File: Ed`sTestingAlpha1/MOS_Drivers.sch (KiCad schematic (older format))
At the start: 6 parts

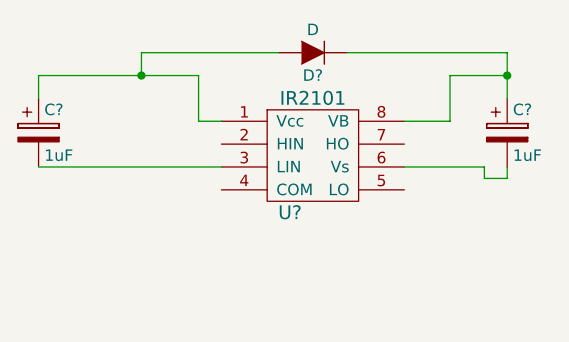
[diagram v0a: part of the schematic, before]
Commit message: Small mods on schematic -- added some pins
Added some docs
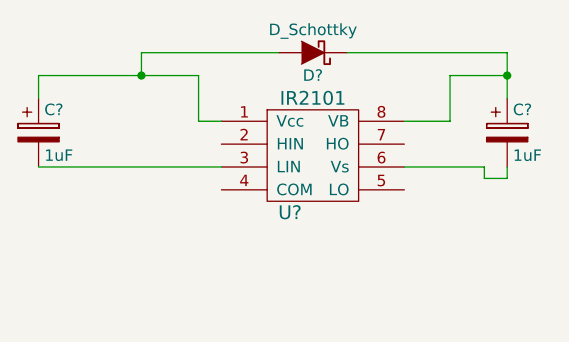
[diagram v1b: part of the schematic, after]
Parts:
- removed D?: D, symbol D
- added D?: D_Schottky, symbol D_Schottky
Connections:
- net at C?.1, U?.1 (Vcc): now also D?.2 (A)
- net at C?.1, U?.8 (VB): now also D?.1 (K)
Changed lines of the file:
@@
 EESchema Schematic File Version 2
+LIBS:BLDC_Driver_1-rescue
 LIBS:power
 LIBS:device
@@
 $EndComp
 $Comp
-L D D?
-U 1 1 5831CCE5
-P 5650 2200
-F 0 "D?" H 5650 2300 50  0000 C CNN
-F 1 "D" H 5650 2100 50  0000 C CNN
-F 2 "" H 5650 2200 50  0000 C CNN
-F 3 "" H 5650 2200 50  0000 C CNN
-	1    5650 2200
-	-1   0    0    1
-$EndComp
-$Comp
 L CP C?
 U 1 1 5831D201
@@
 	4900 2200 4900 2300
 Wire Wire Line
-	4450 2300 5150 2300
+	4450 2300 4900 2300
+Wire Wire Line
+	4900 2300 5150 2300
 Connection ~ 4900 2300
 Wire Wire Line
 	4450 2400 4450 2300
 Wire Wire Line
-	6500 2200 6500 2400
+	6500 2200 6500 2300
+Wire Wire Line
+	6500 2300 6500 2400
 Wire Wire Line
 	6250 2300 6500 2300
@@
 Wire Wire Line
 	6500 2750 6500 2700
+$Comp
+L D_Schottky D?
+U 1 1 5836BF60
+P 5650 2200
+F 0 "D?" H 5650 2300 50  0000 C CNN
+F 1 "D_Schottky" H 5650 2100 50  0000 C CNN
+F 2 "" H 5650 2200 60  0000 C CNN
+F 3 "" H 5650 2200 60  0000 C CNN
+	1    5650 2200
+	-1   0    0    1
+$EndComp
 $EndSCHEMATC
